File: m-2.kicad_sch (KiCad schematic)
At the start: 61 parts, among them J1 Bus_M.2_2199230-6, J2 Bus_M.2_1-2199230-6, M3 Mech_M2_2280_H2.5mm, U2 74LVC2G07_SOT457, U3 74LVC2G07_SOT457, Y1 Oscillator_SMD_32.768kHz_ECS_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

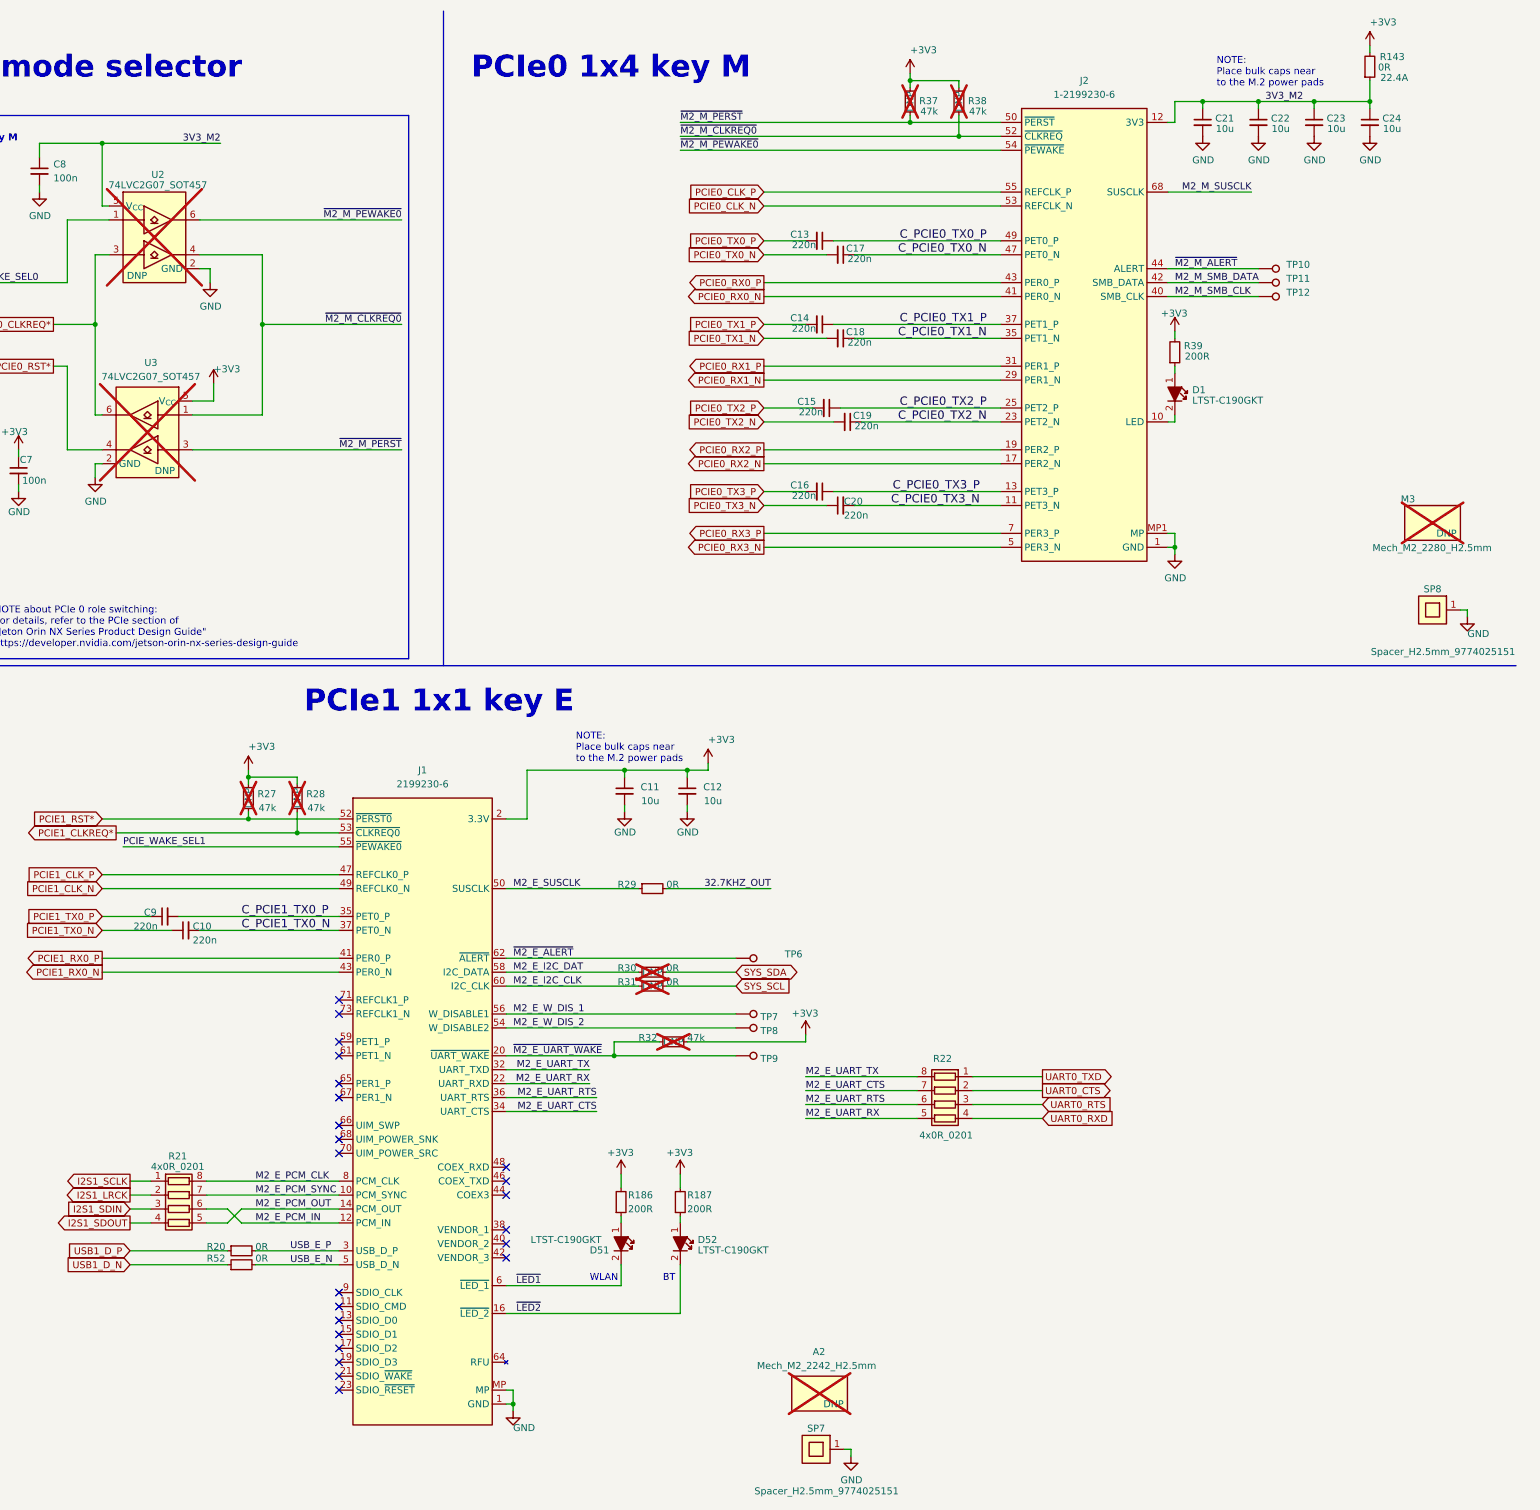
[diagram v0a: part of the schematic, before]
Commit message: 5/16 Commit: Sch Mods added and beginning Development on PCB layout
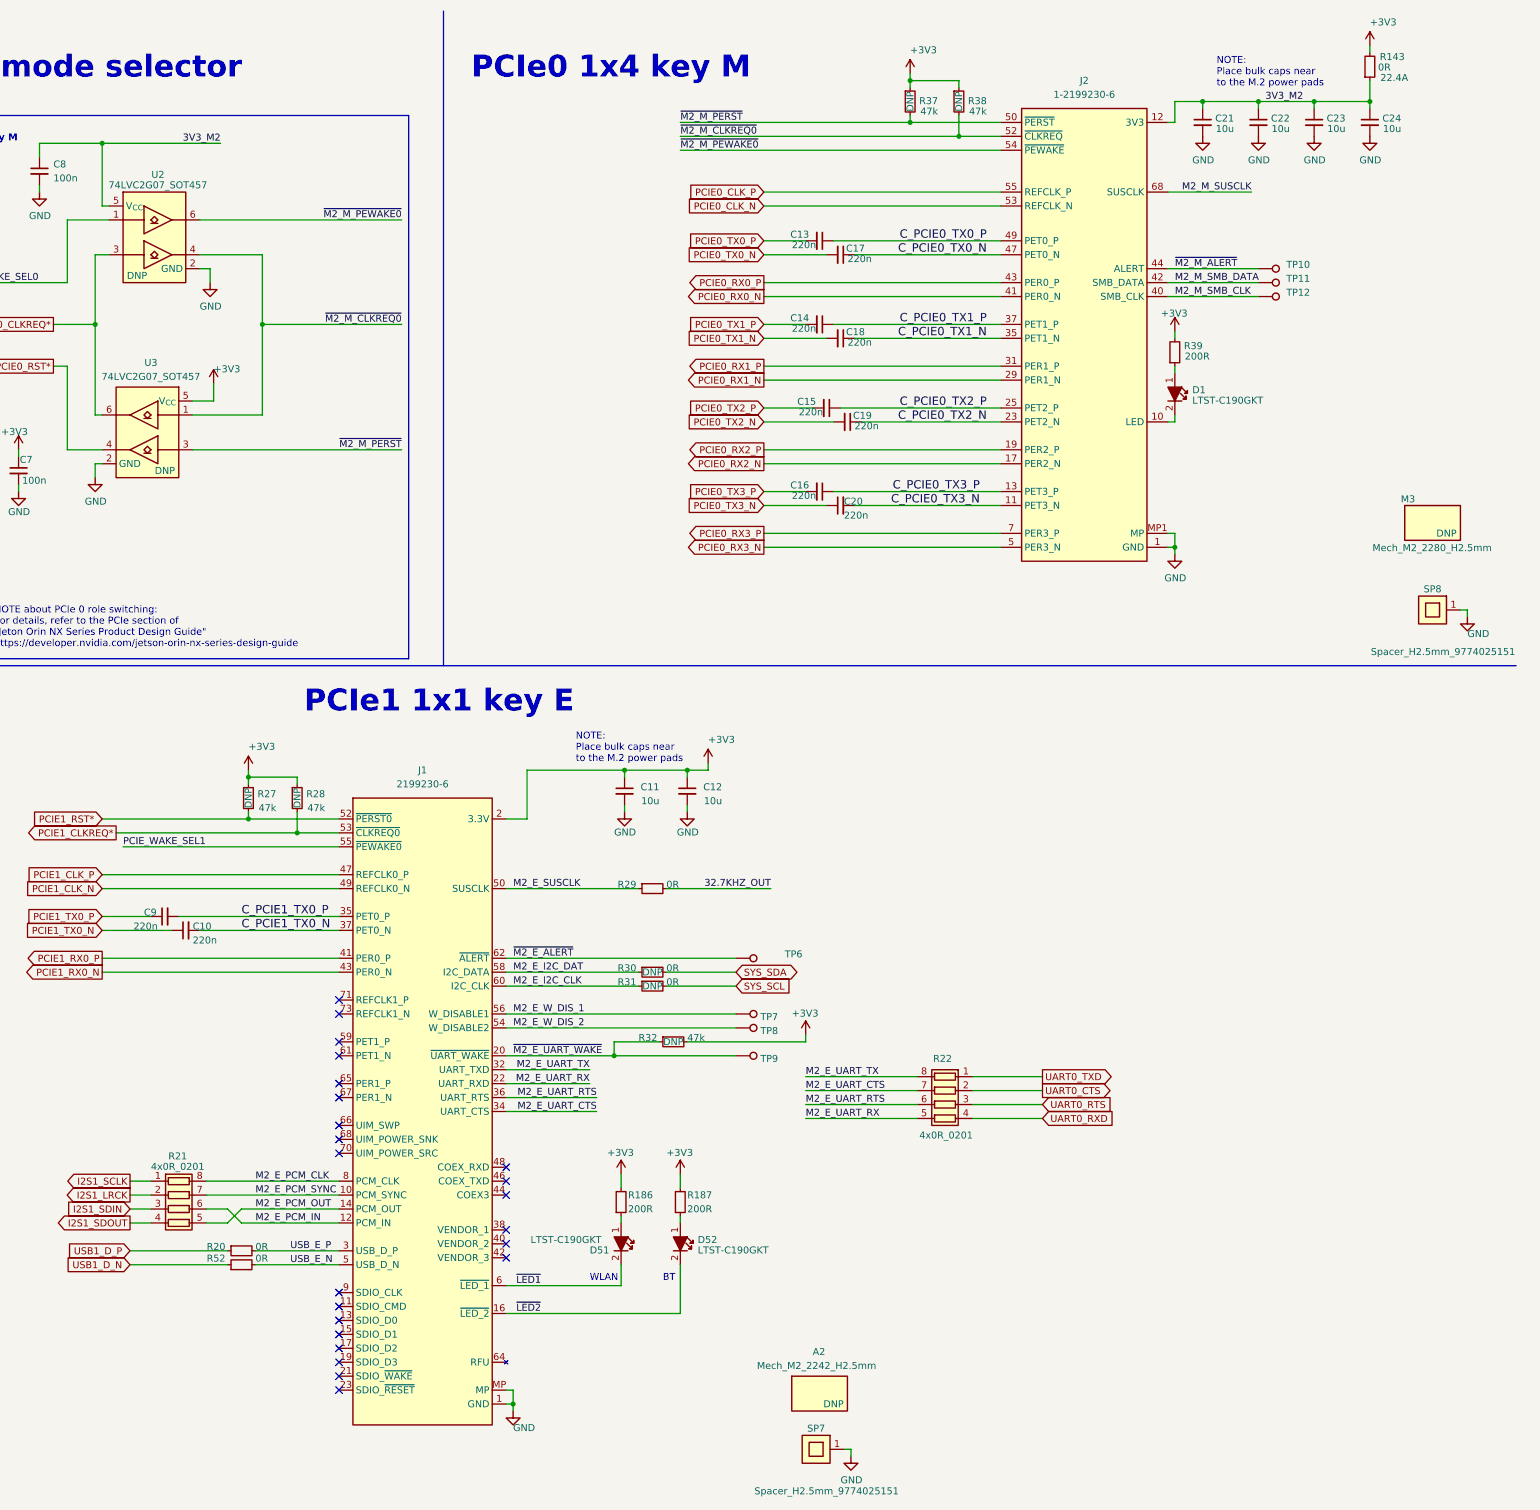
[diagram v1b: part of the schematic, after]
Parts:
- A2, M3, R27, R28, R30, R31, R32, R37, R38, U2, U3: now fitted
